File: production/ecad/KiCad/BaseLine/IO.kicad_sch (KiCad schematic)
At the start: 10 parts, among them J10 LoadCell1, J11 LoadCell2, J12 LoadCell3, J13 LoadCell4, J17 IMU_connector, U12 CD74HC4067M96

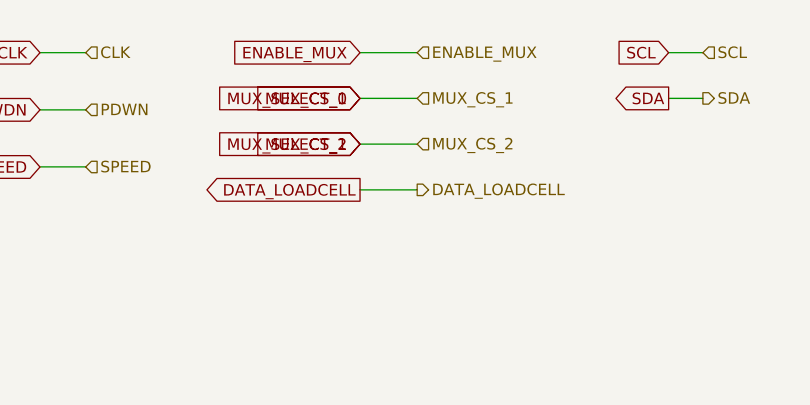
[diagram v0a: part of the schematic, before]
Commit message: fixed labels in I/O
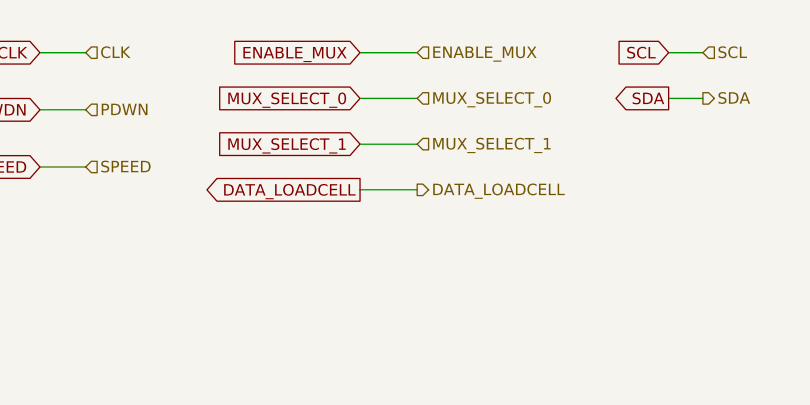
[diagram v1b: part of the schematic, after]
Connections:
- net MUX_CS_1 renamed MUX_SELECT_0
- net MUX_CS_2 renamed MUX_SELECT_1
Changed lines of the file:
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@@
-		)
-	)
-	(global_label "MUX_CS_2"
-		(shape input)
-		(at 83.82 27.94 180)
-		(fields_autoplaced yes)
-		(effects
-			(font
-				(size 1.27 1.27)
-			)
-			(justify right)
-		)
-		(property "Intersheetrefs" "${INTERSHEET_REFS}"
-			(at 71.2192 27.94 0)
-			(effects
-				(font
-					(size 1.27 1.27)
-				)
-				(justify right)
-				(hide yes)
-			)
 		)
 	)
@@
 		)
 	)
-	(global_label "MUX_CS_1"
-		(shape input)
-		(at 83.82 22.86 180)
-		(fields_autoplaced yes)
-		(effects
-			(font
-				(size 1.27 1.27)
-			)
-			(justify right)
-		)
-		(property "Intersheetrefs" "${INTERSHEET_REFS}"
-			(at 71.2192 22.86 0)
-			(effects
-				(font
-					(size 1.27 1.27)
-				)
-				(justify right)
-				(hide yes)
-			)
-		)
-	)
 	(global_label "DOUT_0"
 		(shape output)
@@
 		)
 	)
-	(hierarchical_label "MUX_CS_2"
+	(hierarchical_label "MUX_SELECT_1"
 		(shape input)
 		(at 90.17 27.94 0)
@@
 		)
 	)
-	(hierarchical_label "MUX_CS_1"
+	(hierarchical_label "MUX_SELECT_0"
 		(shape input)
 		(at 90.17 22.86 0)

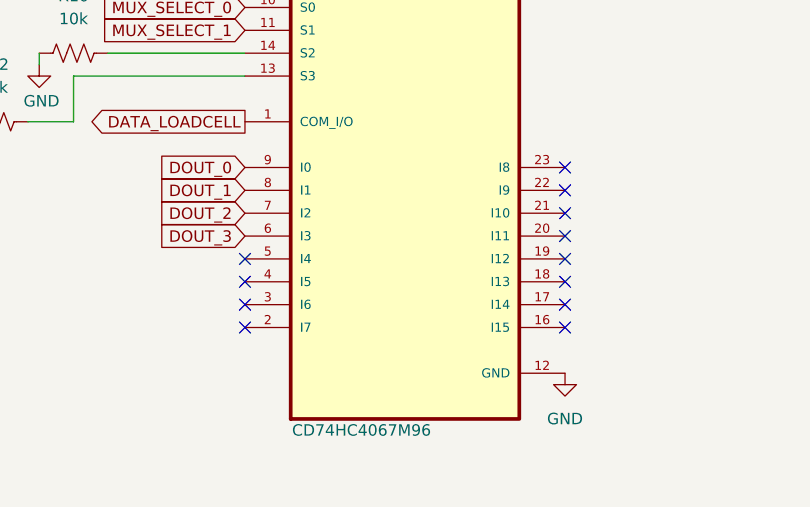
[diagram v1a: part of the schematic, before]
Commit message: grounding unused mux pins
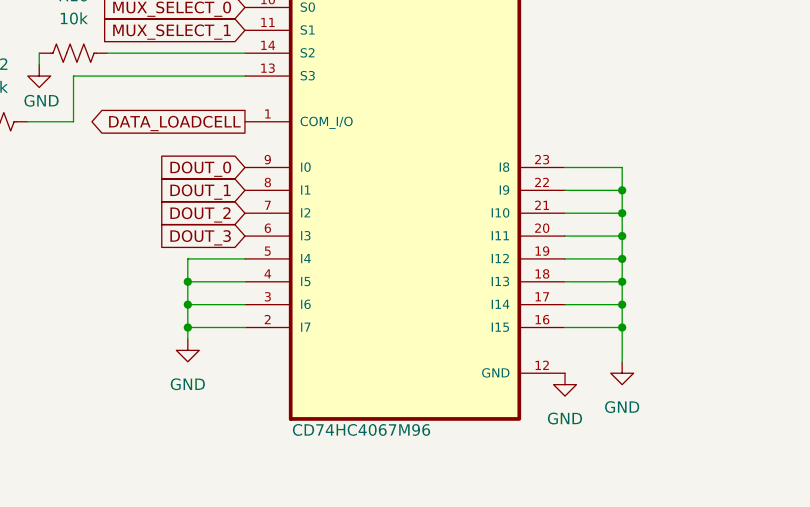
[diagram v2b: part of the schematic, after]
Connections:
- net GND: now also U12.16 (I15), U12.17 (I14), U12.18 (I13), U12.19 (I12), U12.2 (I7), U12.20 (I11), U12.21 (I10), U12.22 (I9), U12.23 (I8), U12.3 (I6), U12.4 (I5), U12.5 (I4)
- no-connect marks 12 -> 0

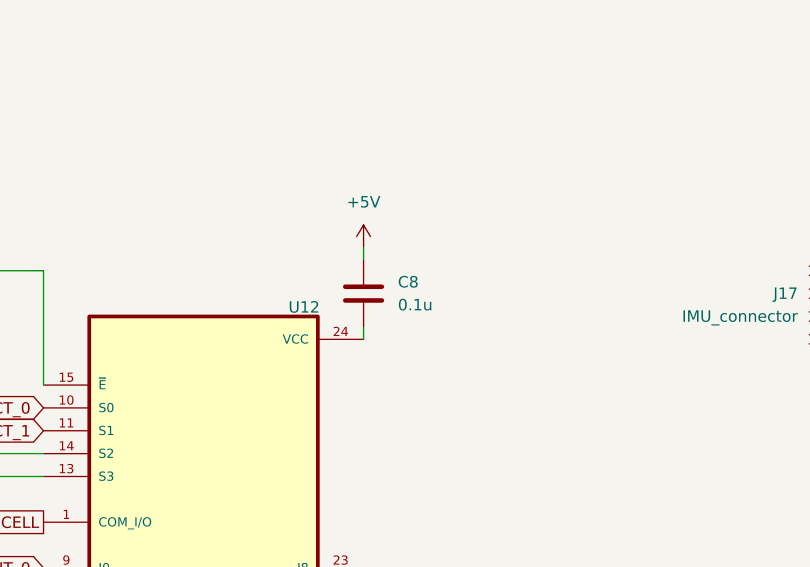
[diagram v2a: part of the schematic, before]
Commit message: Changed capacitor on I/O
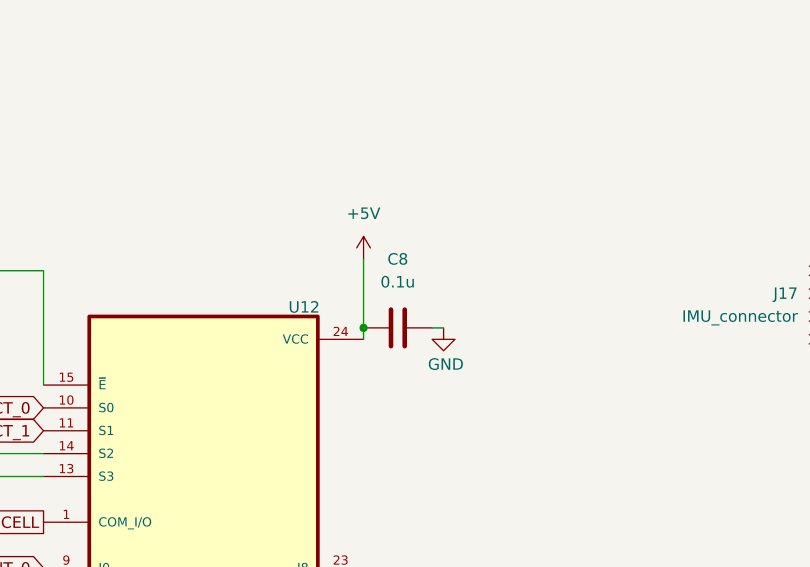
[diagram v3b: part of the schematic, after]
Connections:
- net +5V: now also U12.24 (VCC)
- net GND: now also C8.2
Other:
- moved on the sheet: C8
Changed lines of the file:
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@@
+	)
+	(junction
+		(at 162.56 77.47)
+		(diameter 0)
+		(color 0 0 0 0)
 	)
 	(junction
@@
 	(wire
 		(pts
-			(xy 162.56 68.58) (xy 162.56 69.85)
-		)
-		(stroke
-			(width 0)
-			(type default)
-		)
-	)
-	(wire
-		(pts
 			(xy 168.91 106.68) (xy 168.91 109.22)
 		)
@@
 	(wire
 		(pts
+			(xy 162.56 69.85) (xy 162.56 77.47)
+		)
+		(stroke
+			(width 0)
+			(type default)
+		)
+	)
+	(wire
+		(pts
 			(xy 120.65 121.92) (xy 127 121.92)
 		)
@@
 		(pts
 			(xy 107.95 99.06) (xy 102.87 99.06)
+		)
+		(stroke
+			(width 0)
+			(type default)
+		)
+	)
+	(wire
+		(pts
+			(xy 170.18 77.47) (xy 171.45 77.47)
 		)
 		(stroke
@@
 	(symbol
 		(lib_id "power:+5V")
-		(at 162.56 68.58 0)
+		(at 162.56 69.85 0)
 		(unit 1)
 		(exclude_from_sim no)
@@
 		(fields_autoplaced yes)
 		(property "Reference" "#PWR0100"
-			(at 162.56 72.39 0)
+			(at 162.56 73.66 0)
 			(effects
 				(font
@@
 		)
 		(property "Value" "+5V"
-			(at 162.56 63.5 0)
+			(at 162.56 64.77 0)
 			(effects
 				(font
@@
 		)
 		(property "Footprint" ""
-			(at 162.56 68.58 0)
+			(at 162.56 69.85 0)
 			(effects
 				(font
@@
 		)
 		(property "Datasheet" ""
-			(at 162.56 68.58 0)
+			(at 162.56 69.85 0)
 			(effects
 				(font
@@
 		)
 		(property "Description" "Power symbol creates a global label with name \"+5V\""
-			(at 162.56 68.58 0)
+			(at 162.56 69.85 0)
 			(effects
 				(font
@@
 	(symbol
 		(lib_id "power:GND")
+		(at 171.45 77.47 0)
+		(unit 1)
+		(exclude_from_sim no)
+		(in_bom yes)
+		(on_board yes)
+		(dnp no)
+		(property "Reference" "#PWR033"
+			(at 171.45 83.82 0)
+			(effects
+				(font
+					(size 1.27 1.27)
+				)
+				(hide yes)
+			)
+		)
+		(property "Value" "GND"
+			(at 171.704 81.534 0)
+			(effects
+				(font
+					(size 1.27 1.27)
+				)
+			)
+		)
+		(property "Footprint" ""
+			(at 171.45 77.47 0)
+			(effects
+				(font
+					(size 1.27 1.27)
+				)
+				(hide yes)
+			)
+		)
+		(property "Datasheet" ""
+			(at 171.45 77.47 0)
+			(effects
+				(font
+					(size 1.27 1.27)
+				)
+				(hide yes)
+			)
+		)
+		(property "Description" "Power symbol creates a global label with name \"GND\" , ground"
+			(at 171.45 77.47 0)
+			(effects
+				(font
+					(size 1.27 1.27)
+				)
+				(hide yes)
+			)
+		)
+		(pin "1"
+		)
+		(instances
+			(project "BaseLine"
+				(path "/ba9eda21-3882-41e1-8265-3d8ac781da20/e3080f39-1d26-4bce-b471-534f477eeea5"
+					(reference "#PWR033")
+					(unit 1)
+				)
+			)
+		)
+	)
+	(symbol
+		(lib_id "power:GND")
 		(at 104.14 92.71 0)
 		(unit 1)
@@
 	(symbol
 		(lib_id "Device:C")
-		(at 162.56 73.66 0)
+		(at 166.37 77.47 90)
 		(unit 1)
 		(exclude_from_sim no)
@@
 		(fields_autoplaced yes)
 		(property "Reference" "C8"
-			(at 166.37 72.3899 0)
-			(effects
-				(font
-					(size 1.27 1.27)
-				)
-				(justify left)
+			(at 166.37 69.85 90)
+			(effects
+				(font
+					(size 1.27 1.27)
+				)
 			)
 		)
 		(property "Value" "0.1u"
-			(at 166.37 74.9299 0)
-			(effects
-				(font
-					(size 1.27 1.27)
-				)
-				(justify left)
+			(at 166.37 72.39 90)
+			(effects
+				(font
+					(size 1.27 1.27)
+				)
 			)
 		)
 		(property "Footprint" "Capacitor_SMD:C_0805_2012Metric_Pad1.18x1.45mm_HandSolder"
-			(at 163.5252 77.47 0)
+			(at 170.18 76.5048 0)
 			(effects
 				(font
@@
 		)
 		(property "Datasheet" "~"
-			(at 162.56 73.66 0)
+			(at 166.37 77.47 0)
 			(effects
 				(font
@@
 		)
 		(property "Description" "Unpolarized capacitor"
-			(at 162.56 73.66 0)
-			(effects
-				(font
+			(at 166.37 77.47 0)
+			(effects
+				(font

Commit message: doing some things for layout
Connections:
- net +5V: no longer U12.24 (VCC)
- net GND: no longer C8.2
- new net: C8.2, U12.24 (VCC)
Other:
- moved on the sheet: C8
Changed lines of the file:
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@@
-	)
-	(junction
-		(at 162.56 77.47)
-		(diameter 0)
-		(color 0 0 0 0)
 	)
 	(junction
@@
 	(wire
 		(pts
+			(xy 162.56 68.58) (xy 162.56 69.85)
+		)
+		(stroke
+			(width 0)
+			(type default)
+		)
+	)
+	(wire
+		(pts
 			(xy 168.91 106.68) (xy 168.91 109.22)
 		)
@@
 	(wire
 		(pts
-			(xy 162.56 69.85) (xy 162.56 77.47)
-		)
-		(stroke
-			(width 0)
-			(type default)
-		)
-	)
-	(wire
-		(pts
 			(xy 120.65 121.92) (xy 127 121.92)
 		)
@@
 		(pts
 			(xy 107.95 99.06) (xy 102.87 99.06)
-		)
-		(stroke
-			(width 0)
-			(type default)
-		)
-	)
-	(wire
-		(pts
-			(xy 170.18 77.47) (xy 171.45 77.47)
 		)
 		(stroke
@@
 	(symbol
 		(lib_id "power:+5V")
-		(at 162.56 69.85 0)
+		(at 162.56 68.58 0)
 		(unit 1)
 		(exclude_from_sim no)
@@
 		(fields_autoplaced yes)
 		(property "Reference" "#PWR0100"
-			(at 162.56 73.66 0)
+			(at 162.56 72.39 0)
 			(effects
 				(font
@@
 		)
 		(property "Value" "+5V"
-			(at 162.56 64.77 0)
+			(at 162.56 63.5 0)
 			(effects
 				(font
@@
 		)
 		(property "Footprint" ""
-			(at 162.56 69.85 0)
+			(at 162.56 68.58 0)
 			(effects
 				(font
@@
 		)
 		(property "Datasheet" ""
-			(at 162.56 69.85 0)
+			(at 162.56 68.58 0)
 			(effects
 				(font
@@
 		)
 		(property "Description" "Power symbol creates a global label with name \"+5V\""
-			(at 162.56 69.85 0)
+			(at 162.56 68.58 0)
 			(effects
 				(font
@@
 	(symbol
 		(lib_id "power:GND")
-		(at 171.45 77.47 0)
-		(unit 1)
-		(exclude_from_sim no)
-		(in_bom yes)
-		(on_board yes)
-		(dnp no)
-		(property "Reference" "#PWR033"
-			(at 171.45 83.82 0)
-			(effects
-				(font
-					(size 1.27 1.27)
-				)
-				(hide yes)
-			)
-		)
-		(property "Value" "GND"
-			(at 171.704 81.534 0)
-			(effects
-				(font
-					(size 1.27 1.27)
-				)
-			)
-		)
-		(property "Footprint" ""
-			(at 171.45 77.47 0)
-			(effects
-				(font
-					(size 1.27 1.27)
-				)
-				(hide yes)
-			)
-		)
-		(property "Datasheet" ""
-			(at 171.45 77.47 0)
-			(effects
-				(font
-					(size 1.27 1.27)
-				)
-				(hide yes)
-			)
-		)
-		(property "Description" "Power symbol creates a global label with name \"GND\" , ground"
-			(at 171.45 77.47 0)
-			(effects
-				(font
-					(size 1.27 1.27)
-				)
-				(hide yes)
-			)
-		)
-		(pin "1"
-		)
-		(instances
-			(project "BaseLine"
-				(path "/ba9eda21-3882-41e1-8265-3d8ac781da20/e3080f39-1d26-4bce-b471-534f477eeea5"
-					(reference "#PWR033")
-					(unit 1)
-				)
-			)
-		)
-	)
-	(symbol
-		(lib_id "power:GND")
 		(at 104.14 92.71 0)
 		(unit 1)
@@
 	(symbol
 		(lib_id "Device:C")
-		(at 166.37 77.47 90)
+		(at 162.56 73.66 0)
 		(unit 1)
 		(exclude_from_sim no)
@@
 		(fields_autoplaced yes)
 		(property "Reference" "C8"
-			(at 166.37 69.85 90)
-			(effects
-				(font
-					(size 1.27 1.27)
-				)
+			(at 166.37 72.3899 0)
+			(effects
+				(font
+					(size 1.27 1.27)
+				)
+				(justify left)
 			)
 		)
 		(property "Value" "0.1u"
-			(at 166.37 72.39 90)
-			(effects
-				(font
-					(size 1.27 1.27)
-				)
+			(at 166.37 74.9299 0)
+			(effects
+				(font
+					(size 1.27 1.27)
+				)
+				(justify left)
 			)
 		)
 		(property "Footprint" "Capacitor_SMD:C_0805_2012Metric_Pad1.18x1.45mm_HandSolder"
-			(at 170.18 76.5048 0)
+			(at 163.5252 77.47 0)
 			(effects
 				(font
@@
 		)
 		(property "Datasheet" "~"
-			(at 166.37 77.47 0)
+			(at 162.56 73.66 0)
 			(effects
 				(font
@@
 		)
 		(property "Description" "Unpolarized capacitor"
-			(at 166.37 77.47 0)
-			(effects
-				(font
+			(at 162.56 73.66 0)
+			(effects
+				(font

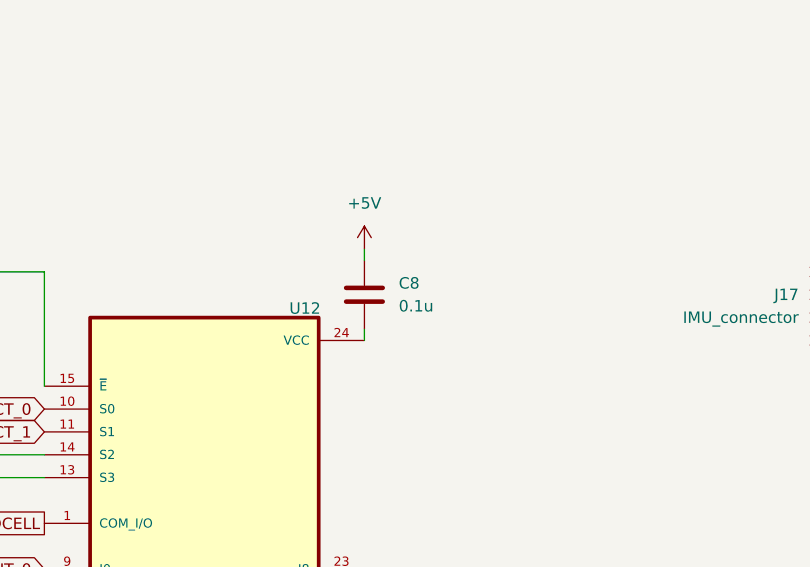
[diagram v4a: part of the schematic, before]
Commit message: Finished PCB draft 1
some errors for USBC footprint and have to fix battery connection planes
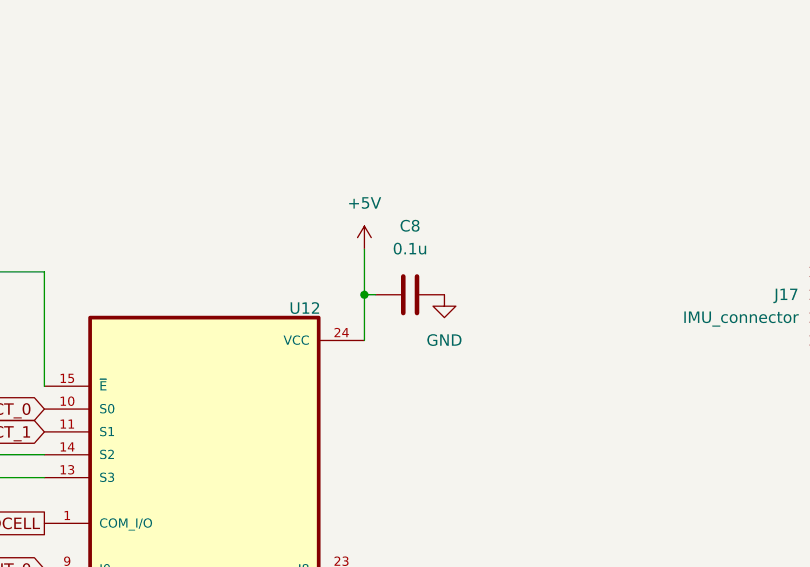
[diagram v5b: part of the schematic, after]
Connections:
- net +5V: now also U12.24 (VCC)
- net GND: now also C8.2
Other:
- moved on the sheet: C8
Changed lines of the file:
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@@
 		(color 0 0 0 0)
 	)
+	(junction
+		(at 162.56 73.66)
+		(diameter 0)
+		(color 0 0 0 0)
+	)
+	(wire
+		(pts
+			(xy 162.56 73.66) (xy 162.56 78.74)
+		)
+		(stroke
+			(width 0)
+			(type default)
+		)
+	)
 	(wire
 		(pts
@@
 	(wire
 		(pts
-			(xy 162.56 68.58) (xy 162.56 69.85)
-		)
-		(stroke
-			(width 0)
-			(type default)
-		)
-	)
-	(wire
-		(pts
 			(xy 168.91 106.68) (xy 168.91 109.22)
 		)
@@
 	(wire
 		(pts
-			(xy 162.56 77.47) (xy 162.56 78.74)
-		)
-		(stroke
-			(width 0)
-			(type default)
-		)
-	)
-	(wire
-		(pts
 			(xy 101.6 71.12) (xy 110.49 71.12)
 		)
@@
 	(wire
 		(pts
+			(xy 162.56 68.58) (xy 162.56 73.66)
+		)
+		(stroke
+			(width 0)
+			(type default)
+		)
+	)
+	(wire
+		(pts
 			(xy 95.25 99.06) (xy 95.25 102.87)
 		)
@@
 		(pts
 			(xy 48.26 24.13) (xy 53.34 24.13)
+		)
+		(stroke
+			(width 0)
+			(type default)
+		)
+	)
+	(wire
+		(pts
+			(xy 162.56 73.66) (xy 163.83 73.66)
 		)
 		(stroke
@@
 	(symbol
 		(lib_id "Device:C")
-		(at 162.56 73.66 0)
+		(at 167.64 73.66 90)
 		(unit 1)
 		(exclude_from_sim no)
@@
 		(fields_autoplaced yes)
 		(property "Reference" "C8"
-			(at 166.37 72.3899 0)
-			(effects
-				(font
-					(size 1.27 1.27)
-				)
-				(justify left)
+			(at 167.64 66.04 90)
+			(effects
+				(font
+					(size 1.27 1.27)
+				)
 			)
 		)
 		(property "Value" "0.1u"
-			(at 166.37 74.9299 0)
-			(effects
-				(font
-					(size 1.27 1.27)
-				)
-				(justify left)
+			(at 167.64 68.58 90)
+			(effects
+				(font
+					(size 1.27 1.27)
+				)
 			)
 		)
 		(property "Footprint" "Capacitor_SMD:C_0805_2012Metric_Pad1.18x1.45mm_HandSolder"
-			(at 163.5252 77.47 0)
+			(at 171.45 72.6948 0)
 			(effects
 				(font
@@
 		)
 		(property "Datasheet" "~"
-			(at 162.56 73.66 0)
+			(at 167.64 73.66 0)
 			(effects
 				(font
@@
 		)
 		(property "Description" "Unpolarized capacitor"
-			(at 162.56 73.66 0)
+			(at 167.64 73.66 0)
 			(effects
 				(font
@@
 					(unit 1)
 				)
+			)
+		)
+	)
+	(symbol
+		(lib_id "power:GND")
+		(at 171.45 73.66 0)
+		(unit 1)
+		(exclude_from_sim no)
+		(in_bom yes)
+		(on_board yes)
+		(dnp no)
+		(fields_autoplaced yes)
+		(property "Reference" "#PWR033"
+			(at 171.45 80.01 0)
+			(effects
+				(font
+					(size 1.27 1.27)
+				)
+				(hide yes)
+			)
+		)
+		(property "Value" "GND"
+			(at 171.45 78.74 0)
+			(effects
+				(font
+					(size 1.27 1.27)
+				)
+			)
+		)
+		(property "Footprint" ""
+			(at 171.45 73.66 0)
+			(effects
+				(font
+					(size 1.27 1.27)
+				)
+				(hide yes)
+			)
+		)
+		(property "Datasheet" ""
+			(at 171.45 73.66 0)
+			(effects
+				(font
+					(size 1.27 1.27)
+				)
+				(hide yes)
+			)
+		)
+		(property "Description" "Power symbol creates a global label with name \"GND\" , ground"
+			(at 171.45 73.66 0)
+			(effects
+				(font
+					(size 1.27 1.27)
+				)
+				(hide yes)
+			)
+		)
+		(pin "1"
+		)
+		(instances
+			(project "BaseLine"
+				(path "/ba9eda21-3882-41e1-8265-3d8ac781da20/e3080f39-1d26-4bce-b471-534f477eeea5"
+					(reference "#PWR033")
+					(unit 1)
+				)
